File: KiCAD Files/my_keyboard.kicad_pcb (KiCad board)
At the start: 2 copper layers, 120 x 120 mm, 43 parts, among them K1 KEYSW, K10 KEYSW, K11 KEYSW, K12 KEYSW, K13 KEYSW, K14 KEYSW, K15 KEYSW, K16 KEYSW, K17 KEYSW, K2 KEYSW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

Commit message: Update PCB
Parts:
- added H1: MountingHole_Pad, MountingHole:MountingHole_4.3mm_M4_Pad_Via, F.Cu at (68.7, 62.5)
- added H2: MountingHole_Pad, MountingHole:MountingHole_4.3mm_M4_Pad_Via, F.Cu at (80.4, 62.5)
- added H3: MountingHole_Pad, MountingHole:MountingHole_4.3mm_M4_Pad_Via, F.Cu at (68.7, 73.1)
- added H4: MountingHole_Pad, MountingHole:MountingHole_4.3mm_M4_Pad_Via, F.Cu at (80.4, 73.1)
- D1, D10, D11, D12, D13, D14, D15, D16, D17, D18, D19, D2, D20, D3, D4, D5, D6, D7, D8, D9: footprint Diode_THT:D_DO-35_SOD27_P10.16mm_Horizontal -> keyboard_parts:D_SOD123_axial
- SW1: footprint Button_Switch_THT:SW_PUSH_6mm -> Button_Switch_SMD:SW_PUSH_4_5.1x5.1mm
- moved D19 94.6 mm to (183.4, 137.0)
- moved D10 94.5 mm to (147.8, 132.6)
- moved D5 92.3 mm to (119.2, 132.6)
- moved D20 79.7 mm to (183.4, 118.0)
- moved D18 75.0 mm to (166.8, 123.0)
- moved D15 71.2 mm to (183.4, 98.9)
- moved D14 68.8 mm to (147.8, 113.5)
- moved D4 68.8 mm to (109.7, 113.5)
- moved D9 68.8 mm to (128.7, 113.5)
- moved D13 46.5 mm to (147.8, 94.5)
- moved D3 46.5 mm to (109.7, 94.5)
- moved D8 46.5 mm to (128.6, 94.5)
- moved D17 33.7 mm to (166.8, 84.9)
- moved D12 24.2 mm to (147.8, 75.4)
- moved D2 24.2 mm to (109.7, 75.4)
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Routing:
- net /col2: track 204.1 -> 0.00 mm
- net /col0: track 165.9 -> 0.00 mm
- net /col1: track 145.9 -> 0.00 mm
- net /col3: track 132.5 -> 0.00 mm
- net GND: track 112.4 -> 0.00 mm
- net Net-(D10-Pad1): track 107.7 -> 0.00 mm
- net /encoder_S3B: track 107.0 -> 0.00 mm
- net /encoder_S2B: track 104.9 -> 0.00 mm
- net Net-(D5-Pad1): track 103.1 -> 0.00 mm
- net /encoder_A3: track 96.4 -> 0.00 mm
- net /encoder_B3: track 93.8 -> 0.00 mm
- net Net-(D18-Pad1): track 84.6 -> 0.00 mm
- net /row0: track 83.8 -> 0.00 mm
- net /row1: track 81.1 -> 0.00 mm
- net Net-(D14-Pad1): track 77.5 -> 0.00 mm
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- removed copper zone on B.Cu, net GND
- removed copper zone on F.Cu, net GND

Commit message: Added KiCAD Library
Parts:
- moved D19 38.1 mm to (182.7, 98.9), turned to 270 degrees
- moved D20 19.1 mm to (182.7, 137.0), turned to 270 degrees
- moved D15 19.1 mm to (182.7, 118.0), turned to 270 degrees
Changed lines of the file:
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@@
   )
   (module keyboard_parts:D_SOD123_axial locked (layer F.Cu)
-    (at 183.356 98.9012)
+    (at 182.721 117.9512 270)
     (attr smd)
-    (fp_text reference D15 (at 0 1.925) (layer F.SilkS)
+    (fp_text reference D15 (at 0 1.925 90) (layer F.SilkS)
       (effects (font (size 0.8 0.8) (thickness 0.15)))
     )
-    (fp_text value DIODE (at 0 -1.925) (layer F.SilkS) hide
+    (fp_text value DIODE (at 0 -1.925 90) (layer F.SilkS) hide
       (effects (font (size 0.8 0.8) (thickness 0.15)))
     )
@@
     (fp_line (start 2.8 -1.2) (end 2.8 1.2) (layer F.SilkS) (width 0.2))
     (fp_line (start 2.8 1.2) (end -3 1.2) (layer F.SilkS) (width 0.2))
-    (pad 2 smd rect (at 1.575 0) (size 1.2 1.2) (layers F.Cu F.Paste F.Mask)
+    (pad 2 smd rect (at 1.575 0 270) (size 1.2 1.2) (layers F.Cu F.Paste F.Mask)
       (net 5 /row4))
-    (pad 1 smd rect (at -1.575 0) (size 1.2 1.2) (layers F.Cu F.Paste F.Mask)
+    (pad 1 smd rect (at -1.575 0 270) (size 1.2 1.2) (layers F.Cu F.Paste F.Mask)
       (net 37 /encoder_S2B))
-    (pad 1 thru_hole rect (at -3.9 0) (size 1.6 1.6) (drill 0.7) (layers *.Cu *.Mask F.SilkS)
+    (pad 1 thru_hole rect (at -3.9 0 270) (size 1.6 1.6) (drill 0.7) (layers *.Cu *.Mask F.SilkS)
       (net 37 /encoder_S2B))
-    (pad 2 thru_hole circle (at 3.9 0) (size 1.6 1.6) (drill 0.7) (layers *.Cu *.Mask F.SilkS)
+    (pad 2 thru_hole circle (at 3.9 0 270) (size 1.6 1.6) (drill 0.7) (layers *.Cu *.Mask F.SilkS)
       (net 5 /row4))
-    (pad 1 smd rect (at -2.7 0) (size 2.5 0.5) (layers F.Cu)
+    (pad 1 smd rect (at -2.7 0 270) (size 2.5 0.5) (layers F.Cu)
       (net 37 /encoder_S2B) (solder_mask_margin -999))
-    (pad 2 smd rect (at 2.7 0) (size 2.5 0.5) (layers F.Cu)
+    (pad 2 smd rect (at 2.7 0 270) (size 2.5 0.5) (layers F.Cu)
       (net 5 /row4) (solder_mask_margin -999))
   )
@@
   )
   (module keyboard_parts:D_SOD123_axial (layer F.Cu)
-    (at 183.356 137.0012)
+    (at 182.721 98.9012 270)
     (attr smd)
-    (fp_text reference D19 (at 0 1.925) (layer F.SilkS)
+    (fp_text reference D19 (at 0 1.925 90) (layer F.SilkS)
       (effects (font (size 0.8 0.8) (thickness 0.15)))
     )
-    (fp_text value DIODE (at 0 -1.925) (layer F.SilkS) hide
+    (fp_text value DIODE (at 0 -1.925 90) (layer F.SilkS) hide
       (effects (font (size 0.8 0.8) (thickness 0.15)))
     )
@@
     (fp_line (start -2.45 -1.2) (end -2.45 1.2) (layer F.SilkS) (width 0.2))
     (fp_line (start -2.275 -1.2) (end -2.275 1.2) (layer F.SilkS) (width 0.2))
-    (pad 2 smd rect (at 2.7 0) (size 2.5 0.5) (layers F.Cu)
+    (pad 2 smd rect (at 2.7 0 270) (size 2.5 0.5) (layers F.Cu)
       (net 4 /row3) (solder_mask_margin -999))
-    (pad 1 smd rect (at -2.7 0) (size 2.5 0.5) (layers F.Cu)
+    (pad 1 smd rect (at -2.7 0 270) (size 2.5 0.5) (layers F.Cu)
       (net 38 /encoder_S1B) (solder_mask_margin -999))
-    (pad 2 thru_hole circle (at 3.9 0) (size 1.6 1.6) (drill 0.7) (layers *.Cu *.Mask F.SilkS)
+    (pad 2 thru_hole circle (at 3.9 0 270) (size 1.6 1.6) (drill 0.7) (layers *.Cu *.Mask F.SilkS)
       (net 4 /row3))
-    (pad 1 thru_hole rect (at -3.9 0) (size 1.6 1.6) (drill 0.7) (layers *.Cu *.Mask F.SilkS)
+    (pad 1 thru_hole rect (at -3.9 0 270) (size 1.6 1.6) (drill 0.7) (layers *.Cu *.Mask F.SilkS)
       (net 38 /encoder_S1B))
-    (pad 1 smd rect (at -1.575 0) (size 1.2 1.2) (layers F.Cu F.Paste F.Mask)
+    (pad 1 smd rect (at -1.575 0 270) (size 1.2 1.2) (layers F.Cu F.Paste F.Mask)
       (net 38 /encoder_S1B))
-    (pad 2 smd rect (at 1.575 0) (size 1.2 1.2) (layers F.Cu F.Paste F.Mask)
+    (pad 2 smd rect (at 1.575 0 270) (size 1.2 1.2) (layers F.Cu F.Paste F.Mask)
       (net 4 /row3))
   )
   (module keyboard_parts:D_SOD123_axial (layer F.Cu)
-    (at 183.356 117.9512)
+    (at 182.721 137.0012 270)
     (attr smd)
-    (fp_text reference D20 (at 0 1.925) (layer F.SilkS)
+    (fp_text reference D20 (at 0 1.925 90) (layer F.SilkS)
       (effects (font (size 0.8 0.8) (thickness 0.15)))
     )
-    (fp_text value DIODE (at 0 -1.925) (layer F.SilkS) hide
+    (fp_text value DIODE (at 0 -1.925 90) (layer F.SilkS) hide
       (effects (font (size 0.8 0.8) (thickness 0.15)))
     )
@@
     (fp_line (start -2.45 -1.2) (end -2.45 1.2) (layer F.SilkS) (width 0.2))
     (fp_line (start -2.275 -1.2) (end -2.275 1.2) (layer F.SilkS) (width 0.2))
-    (pad 2 smd rect (at 2.7 0) (size 2.5 0.5) (layers F.Cu)
+    (pad 2 smd rect (at 2.7 0 270) (size 2.5 0.5) (layers F.Cu)
       (net 5 /row4) (solder_mask_margin -999))
-    (pad 1 smd rect (at -2.7 0) (size 2.5 0.5) (layers F.Cu)
+    (pad 1 smd rect (at -2.7 0 270) (size 2.5 0.5) (layers F.Cu)
       (net 39 /encoder_S3B) (solder_mask_margin -999))
-    (pad 2 thru_hole circle (at 3.9 0) (size 1.6 1.6) (drill 0.7) (layers *.Cu *.Mask F.SilkS)
+    (pad 2 thru_hole circle (at 3.9 0 270) (size 1.6 1.6) (drill 0.7) (layers *.Cu *.Mask F.SilkS)
       (net 5 /row4))
-    (pad 1 thru_hole rect (at -3.9 0) (size 1.6 1.6) (drill 0.7) (layers *.Cu *.Mask F.SilkS)
+    (pad 1 thru_hole rect (at -3.9 0 270) (size 1.6 1.6) (drill 0.7) (layers *.Cu *.Mask F.SilkS)
       (net 39 /encoder_S3B))
-    (pad 1 smd rect (at -1.575 0) (size 1.2 1.2) (layers F.Cu F.Paste F.Mask)
+    (pad 1 smd rect (at -1.575 0 270) (size 1.2 1.2) (layers F.Cu F.Paste F.Mask)
       (net 39 /encoder_S3B))
-    (pad 2 smd rect (at 1.575 0) (size 1.2 1.2) (layers F.Cu F.Paste F.Mask)
+    (pad 2 smd rect (at 1.575 0 270) (size 1.2 1.2) (layers F.Cu F.Paste F.Mask)
       (net 5 /row4))
   )

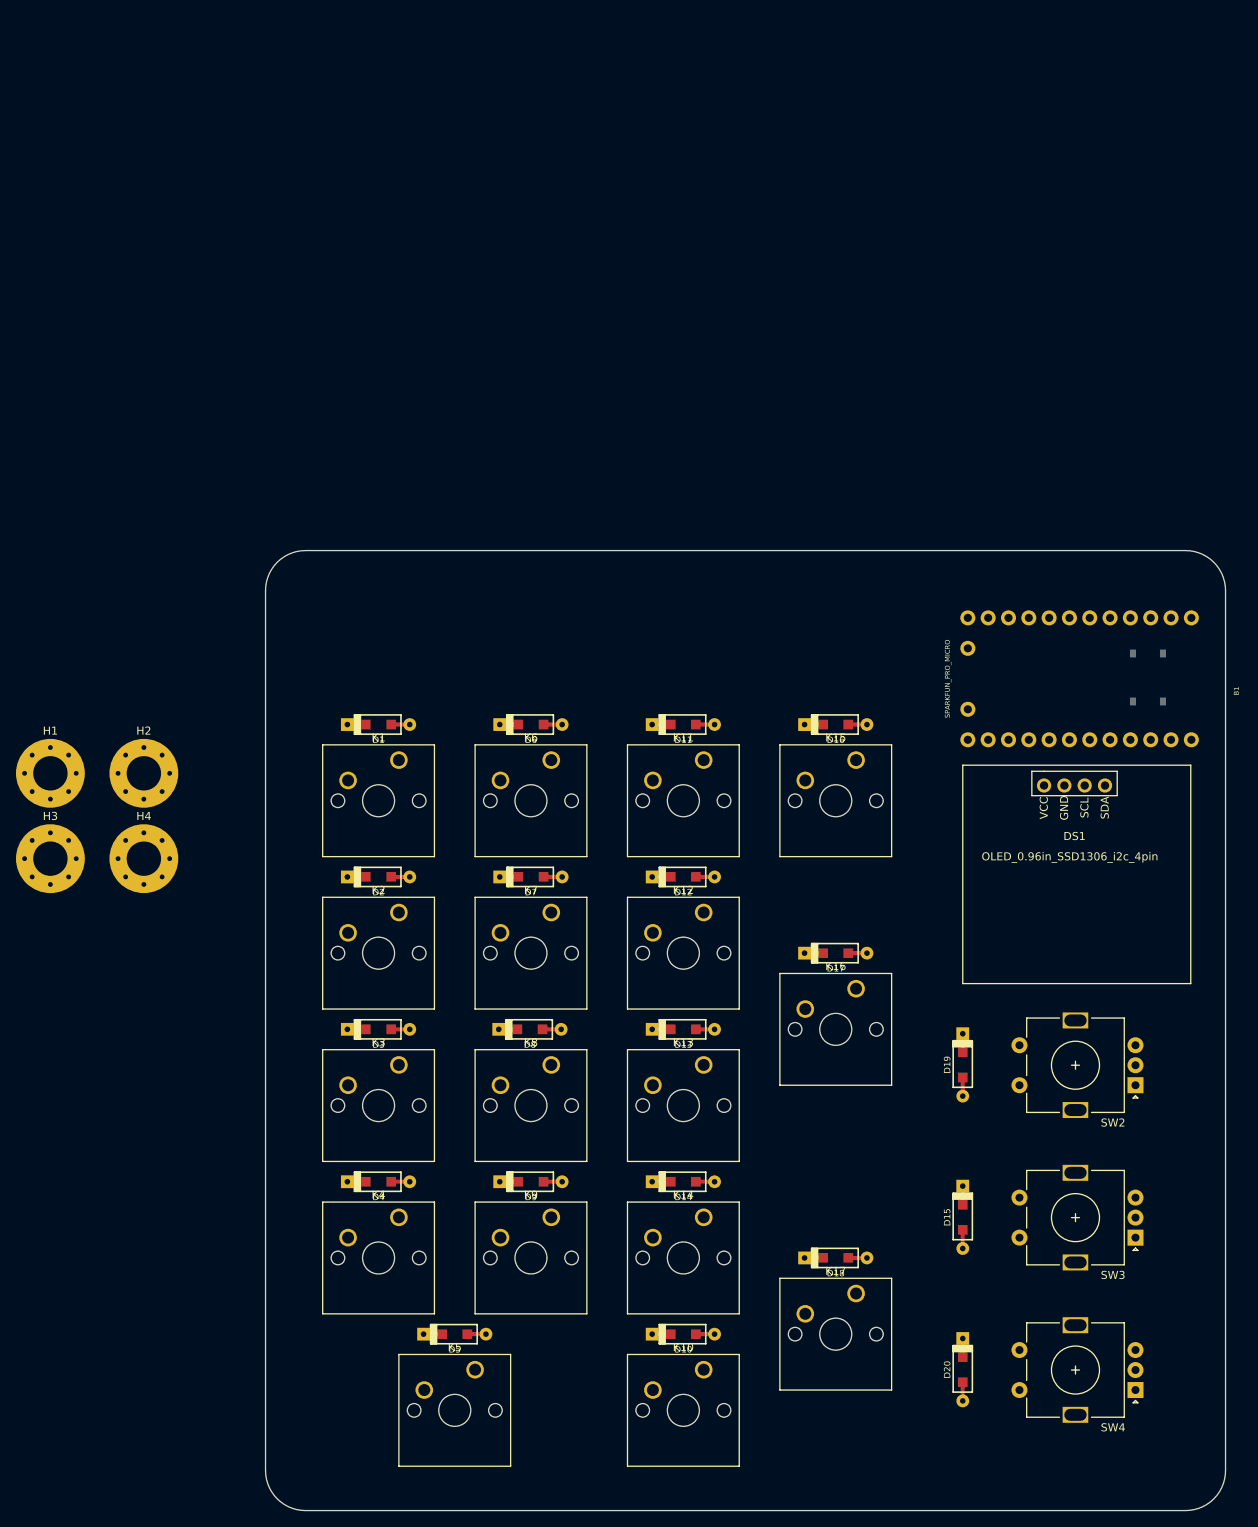
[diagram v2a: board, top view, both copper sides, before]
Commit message: Fixed Diode Issue
Previously used wrong diode symbol meant for simulation not design.
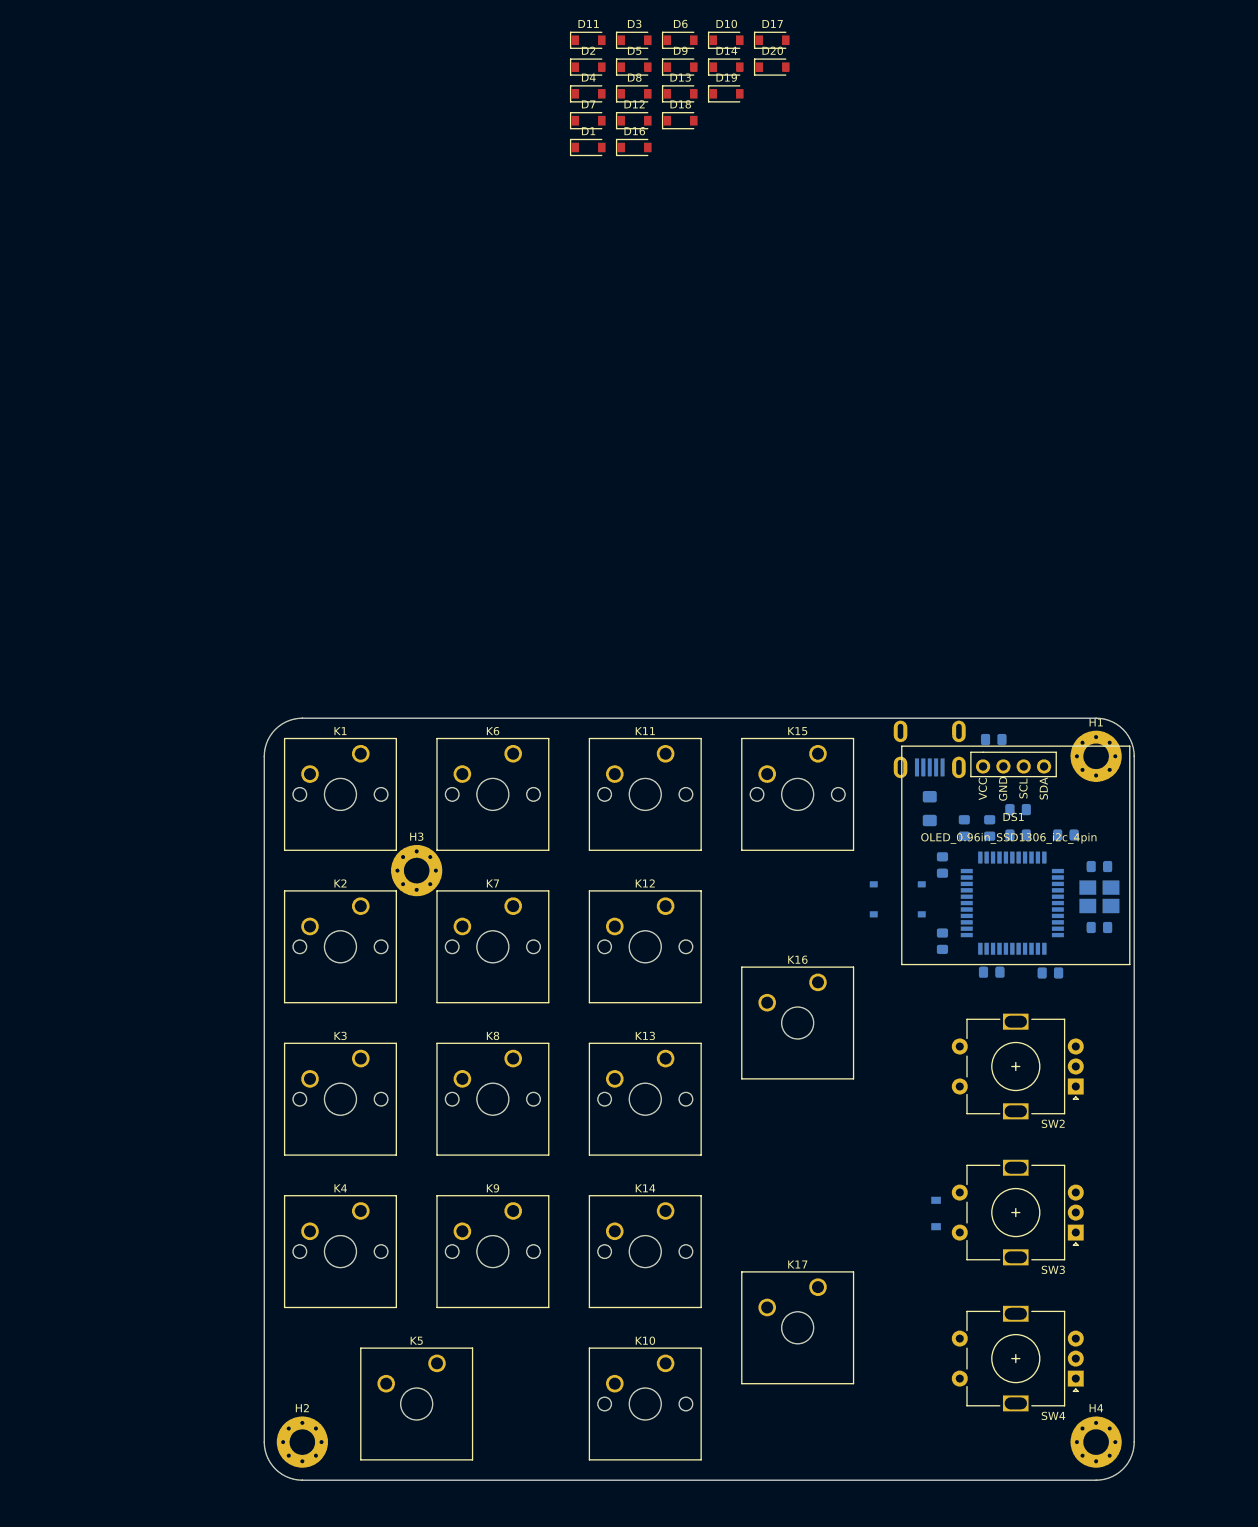
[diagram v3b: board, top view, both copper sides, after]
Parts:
- removed B1: SPARKFUN_PRO_MICRO, SparkFun:SPARKFUN_PRO_MICRO
- added C1: 22pF, Capacitor_SMD:C_0805_2012Metric_Pad1.15x1.40mm_HandSolder, B.Cu at (199.8, 74.1)
- added C2: 22pF, Capacitor_SMD:C_0805_2012Metric_Pad1.15x1.40mm_HandSolder, B.Cu at (199.8, 81.7)
- added C3: 0.1uF, Capacitor_SMD:C_0805_2012Metric_Pad1.15x1.40mm_HandSolder, B.Cu at (193.7, 87.4)
- added C4: 0.1uF, Capacitor_SMD:C_0805_2012Metric_Pad1.15x1.40mm_HandSolder, B.Cu at (180.2, 83.4)
- added C5: 0.1uF, Capacitor_SMD:C_0805_2012Metric_Pad1.15x1.40mm_HandSolder, B.Cu at (180.2, 73.9)
- added C6: 1uF, Capacitor_SMD:C_0805_2012Metric_Pad1.15x1.40mm_HandSolder, B.Cu at (189.6, 70.2)
- added C7: 0.1uF, Capacitor_SMD:C_0805_2012Metric_Pad1.15x1.40mm_HandSolder, B.Cu at (189.6, 67.0)
- added C8: 10uF, Capacitor_SMD:C_0805_2012Metric_Pad1.15x1.40mm_HandSolder, B.Cu at (186.6, 58.2)
- added F1: 500 mA, Fuse:Fuse_1206_3216Metric_Pad1.42x1.75mm_HandSolder, B.Cu at (178.6, 66.9)
- added J1: USB_B_Mini, random-keyboard-parts:Molex-0548190589, B.Cu at (178.6, 57.2)
- added R1: 22, Resistor_SMD:R_0805_2012Metric_Pad1.15x1.40mm_HandSolder, B.Cu at (186.1, 69.3)
- added R2: 22, Resistor_SMD:R_0805_2012Metric_Pad1.15x1.40mm_HandSolder, B.Cu at (182.9, 69.3)
- added R3: 10k, Resistor_SMD:R_0805_2012Metric_Pad1.15x1.40mm_HandSolder, B.Cu at (195.6, 70.2)
- added R4: 10k, Resistor_SMD:R_0805_2012Metric_Pad1.15x1.40mm_HandSolder, B.Cu at (186.3, 87.3)
- added U1: ATmega32U4-AU, Package_QFP:TQFP-44_10x10mm_P0.8mm, B.Cu at (188.9, 78.7)
- added Y1: 16MHz, Crystal:Crystal_SMD_3225-4Pin_3.2x2.5mm_HandSoldering, B.Cu at (199.8, 77.9)
- D1, D10, D11, D12, D13, D14, D16, D17, D18, D19, D2, D20, D3, D4, D5, D6, D7, D8, D9: footprint keyboard_parts:D_SOD123_axial -> Diode_SMD:D_SOD-123
- D15: footprint keyboard_parts:D_SOD123_axial -> Diode_SMD:D_SOD-123; moved to B.Cu
- H1, H2, H3, H4: footprint MountingHole:MountingHole_4.3mm_M4_Pad_Via -> MountingHole:MountingHole_3.2mm_M3_Pad_Via
- K16, K17: footprint Button_Switch_Keyboard:SW_Cherry_MX_1.00u_PCB -> Button_Switch_Keyboard:SW_Cherry_MX_2.00u_Vertical_Plate
- K5: footprint Button_Switch_Keyboard:SW_Cherry_MX_1.00u_PCB -> Button_Switch_Keyboard:SW_Cherry_MX_2.00u_Plate
- moved D20 164.6 mm to (158.9, -25.8), turned to 0 degrees
- moved D10 161.8 mm to (153.2, -29.2)
- moved D5 160.0 mm to (141.7, -25.8)
- moved D18 143.5 mm to (147.4, -19.1)
- moved D9 140.6 mm to (147.4, -25.8)
- moved H4 139.6 mm to (199.4, 146.0)
- moved D14 139.4 mm to (153.2, -25.8)
- moved D4 138.5 mm to (135.9, -22.5)
- moved H1 130.7 mm to (199.4, 60.3)
- moved D3 127.7 mm to (141.7, -29.2)
- moved D19 124.9 mm to (153.2, -22.5), turned to 0 degrees
- moved D8 117.7 mm to (141.7, -22.5)
- moved D13 116.9 mm to (147.4, -22.5)
- moved D17 114.4 mm to (158.9, -29.2)
- moved D2 104.6 mm to (135.9, -25.8)
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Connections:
- net /col2 renamed row2
- net /row0 renamed row0
- net /row1 renamed row1
- net /row3 renamed row3
- net /row4 renamed row4
- DS1 pad 1: VCC -> +5V
- SW1 pad 1: /RESET_SW -> GND
- SW1 pad 2: GND -> Net-(R3-Pad2)
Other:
- board size 120 x 120 mm -> 108.7 x 95.3 mm
- net class Default: trace_width 0.25 -> 0.254
- net class POWER added: clearance 0.2, trace_width 0.381, via_dia 0.8, via_drill 0.4
